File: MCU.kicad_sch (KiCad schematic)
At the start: 79 parts, among them J1301 Conn_01x02_Pin, J1302 JTAG, J1303 JTAG, U1301 ADG1607xCP, U1302 ADG1607xCP, U1303 LP38690SDX-3.3/NOPB, U1304 MSP430FR5969IRGZR, U1305 MSP430FR5969IRGZR, U1306 TCAN4551RGYRQ1

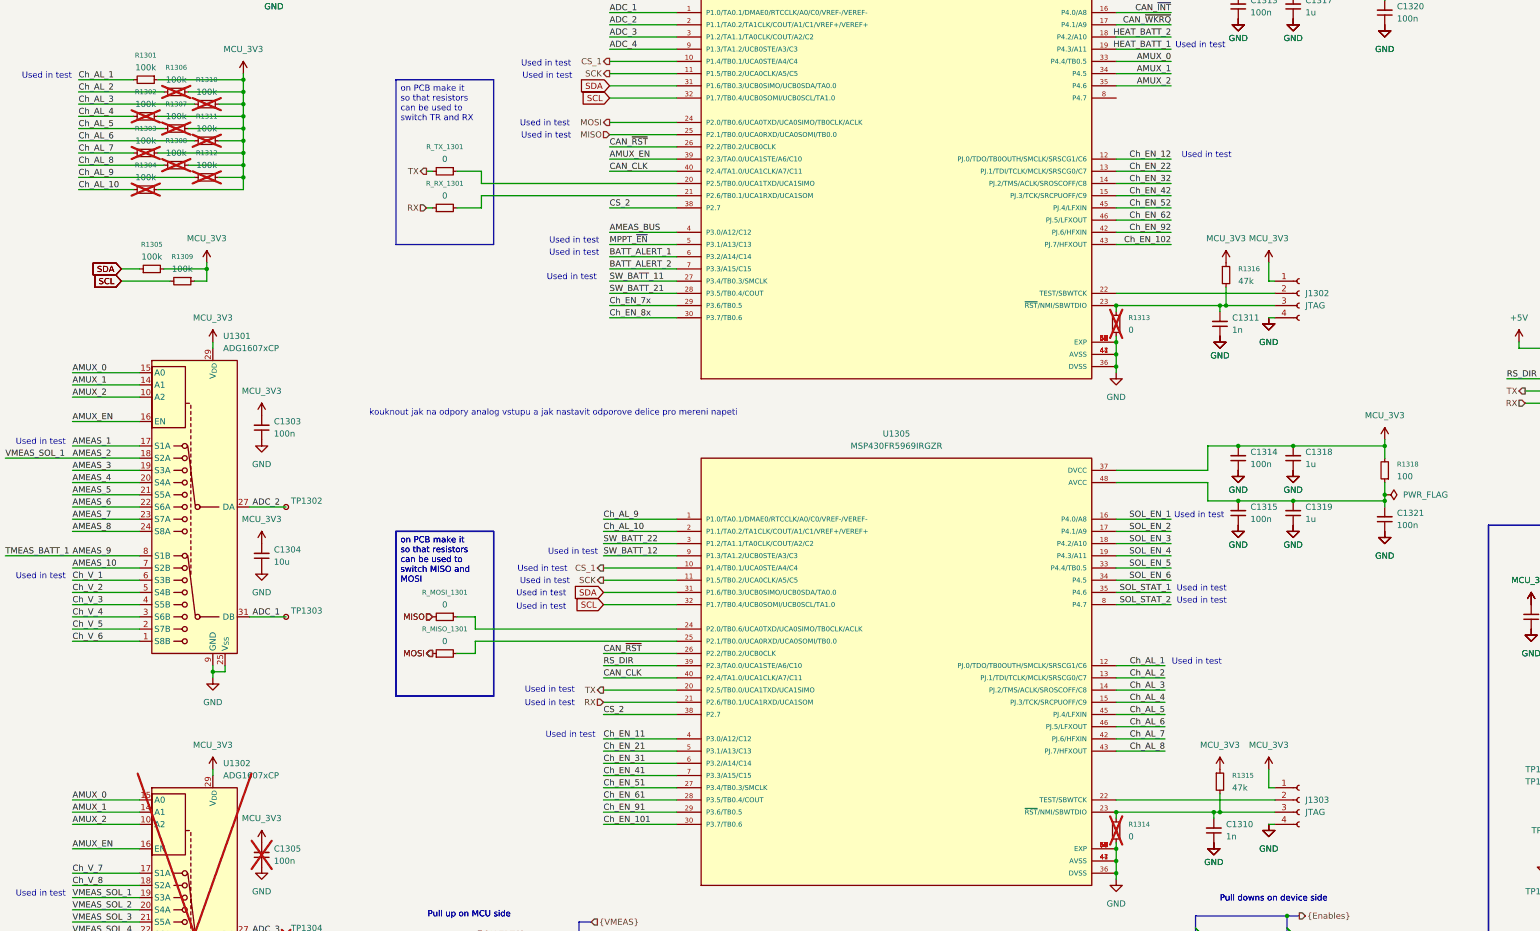
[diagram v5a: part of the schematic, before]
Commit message: Minor changes to acomodate jlcpcb guidelines, this version ordered
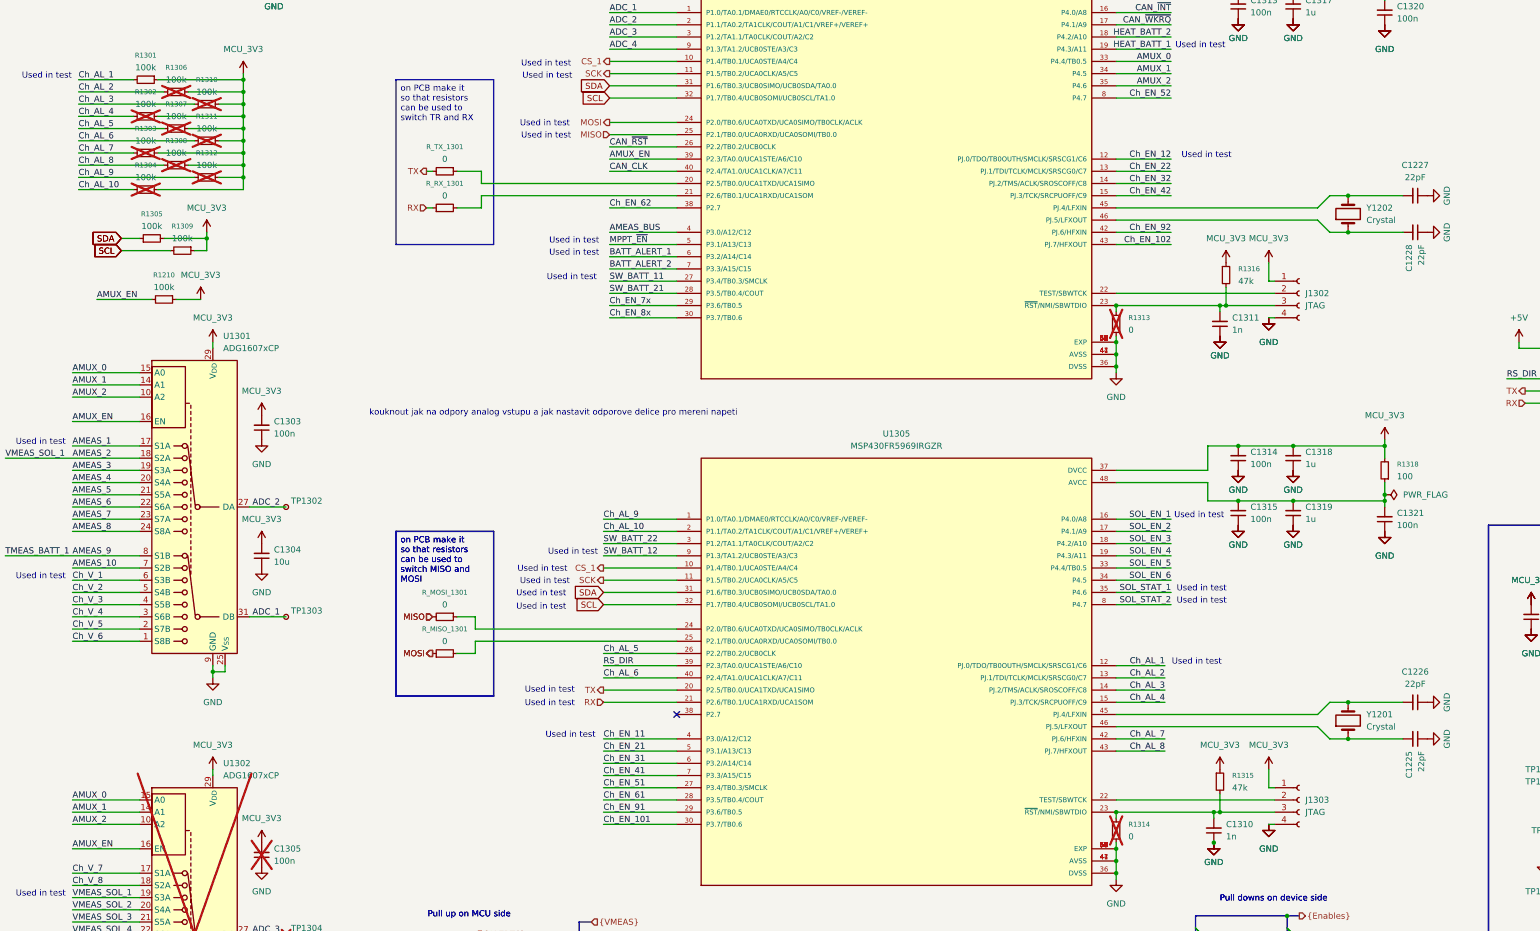
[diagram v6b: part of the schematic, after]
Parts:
- added C1225, C1226, C1227, C1228: 22pF, Capacitor_SMD:C_0603_1608Metric_Pad1.08x0.95mm_HandSolder, symbol Device:C_Small
- added R1210: 100k, Resistor_SMD:R_0603_1608Metric_Pad0.98x0.95mm_HandSolder, symbol Device:R_Small
- added Y1201, Y1202: Crystal, Crystal:Crystal_SMD_2012-2Pin_2.0x1.2mm_HandSoldering, symbol Device:Crystal
- C1304, C1323, C1324: footprint Capacitor_SMD:C_0603_1608Metric_Pad1.08x0.95mm_HandSolder -> Capacitor_SMD:C_1206_3216Metric_Pad1.33x1.80mm_HandSolder
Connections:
- net AMUX_EN: now also R1210.2
- net CAN_CLK: no longer U1305.40 (P2.4/TA1.0/UCA1CLK/A7/C11)
- net CAN_~{RST}: no longer U1305.26 (P2.2/TB0.2/UCB0CLK)
- net Ch_AL_5: now also U1305.26 (P2.2/TB0.2/UCB0CLK); no longer U1305.45 (PJ.4/LFXIN)
- net Ch_AL_6: now also U1305.40 (P2.4/TA1.0/UCA1CLK/A7/C11); no longer U1305.46 (PJ.5/LFXOUT)
- net Ch_EN_52: now also U1304.8 (P4.7); no longer U1304.45 (PJ.4/LFXIN)
- net Ch_EN_62: now also U1304.38 (P2.7); no longer U1304.46 (PJ.5/LFXOUT)
- net GND: now also C1225.1, C1226.1, C1227.1, C1228.1
- net MCU_3V3: now also R1210.1
- net CS_2: no longer names the net of U1305.38 (P2.7)
- net CS_2: no longer U1304.38 (P2.7)
- new net: C1227.2, U1304.45 (PJ.4/LFXIN), Y1202.2
- new net: C1228.2, U1304.46 (PJ.5/LFXOUT), Y1202.1
- new net: C1226.2, U1305.45 (PJ.4/LFXIN), Y1201.2
- new net: C1225.2, U1305.46 (PJ.5/LFXOUT), Y1201.1
- no-connect marks 3 -> 4
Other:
- moved on the sheet: R1305, R1309

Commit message: changes based on test board manufacturing, mostly added voltage dividers
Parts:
- added R1211: 300k, Resistor_SMD:R_0603_1608Metric_Pad0.98x0.95mm_HandSolder, symbol Device:R_Small
- added R1212: 100k, Resistor_SMD:R_0603_1608Metric_Pad0.98x0.95mm_HandSolder, symbol Device:R_Small
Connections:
- net GND: now also R1212.1
- net VBUS: now also R1211.1
- net BATT_BOOT: now reaches U1305.38 (P2.7)
- new net 5V_DCDC_1/EN: R1211.2, R1212.2
- no-connect marks 4 -> 3
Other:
- note added: "EN max 7V needs voltage divider"
- note added: "čast tohoto napajni je objevuje na MCU3V3"
- moved on the sheet: C1301, C1302, C1307, C1308, C1309, J1301, TP1301, TP1306, U1303

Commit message: progress on CORE pcb
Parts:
- removed TP1304, TP1305: ~, TestPoint:TestPoint_Pad_1.0x1.0mm, symbol Connector:TestPoint_Small
- C923: renamed from C1326; now not fitted; now left out of the parts list
- C928: renamed from C1305; now fitted; now in the parts list
- C931: renamed from C1306; footprint Capacitor_SMD:C_0603_1608Metric_Pad1.08x0.95mm_HandSolder -> Capacitor_SMD:C_1206_3216Metric_Pad1.33x1.80mm_HandSolder; now fitted; now in the parts list
- J902: renamed from J1302; footprint Connector_PinSocket_2.54mm:PinSocket_1x04_P2.54mm_Vertical -> Connector_Molex:Molex_PicoBlade_53261-0471_1x04-1MP_P1.25mm_Horizontal
- J903: renamed from J1303; footprint Connector_PinSocket_2.54mm:PinSocket_1x04_P2.54mm_Vertical -> Connector_Molex:Molex_PicoBlade_53261-0471_1x04-1MP_P1.25mm_Horizontal
- R905: renamed from R1306; now fitted; now in the parts list
- R906: renamed from R1310; now fitted; now in the parts list
- R907: renamed from R1302; now fitted; now in the parts list
- R908: renamed from R1307; now fitted; now in the parts list
- R909: renamed from R1311; now fitted; now in the parts list
- R910: renamed from R1303; now fitted; now in the parts list
- R911: renamed from R1308; now fitted; now in the parts list
- R912: renamed from R1312; now fitted; now in the parts list
- R913: renamed from R1304; now fitted; now in the parts list
- U906: renamed from U1302; now fitted; now in the parts list
- renumbered C1301 to C901, C1302 to C902, C1308 to C903, C1309 to C904, C1307 to C905, C1312 to C906, C1316 to C907, C1313 to C908, C1317 to C909, C1320 to C910, C1227 to C911, C1228 to C912, C1311 to C913, C1303 to C914, C1314 to C915, C1318 to C916, C1315 to C917, C1319 to C918, C1321 to C919, C1304 to C920, C1322 to C921, C1323 to C922, C1324 to C924, C1226 to C925, C1225 to C926, C1310 to C927, C1327 to C929, C1325 to C930, J1301 to J901, R1211 to R901, R1212 to R902, R1317 to R903, R1301 to R904, R1305 to R914, R1309 to R915, R1316 to R916, R1210 to R917, R1313 to R918, R1318 to R919, R1319 to R920, R1315 to R921, R1314 to R922, R1320 to R923, R1321 to R924, R_MISO_1301 to R_MISO_901, R_MOSI_1301 to R_MOSI_901, R_RX_1301 to R_RX_901, R_TX_1301 to R_TX_901, TP1301 to TP901, TP1306 to TP902, TP1302 to TP903, TP1303 to TP904, TP1315 to TP905, TP1316 to TP906, TP1318 to TP907, TP1317 to TP908, TP1307 to TP910, TP1308 to TP911, TP1309 to TP912, TP1310 to TP913, TP1313 to TP914, TP1311 to TP915, TP1314 to TP916, TP1312 to TP917, U1303 to U901, U1304 to U902, U1301 to U903, U1305 to U904, U1306 to U905, Y1202 to Y901, Y1201 to Y902
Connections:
- net RX: now also U904.20 (P2.5/TB0.0/UCA1TXD/UCA1SIMO); no longer U904.21 (P2.6/TB0.1/UCA1RXD/UCA1SOM)
- net TX: now also U904.21 (P2.6/TB0.1/UCA1RXD/UCA1SOM); no longer U904.20 (P2.5/TB0.0/UCA1TXD/UCA1SIMO)
- net TX_MCU: now reaches R_TX_901.1, U902.20 (P2.5/TB0.0/UCA1TXD/UCA1SIMO)
- net MISO_MCU: now reaches R_MOSI_901.1, U904.24 (P2.0/TB0.6/UCA0TXD/UCA0SIMO/TB0CLK/ACLK)
- net MOSI_MCU: now reaches R_MISO_901.2, U904.25 (P2.1/TB0.0/UCA0RXD/UCA0SOMI/TB0.0)
- net RX_MCU: now reaches R_RX_901.2, U902.21 (P2.6/TB0.1/UCA1RXD/UCA1SOM)
